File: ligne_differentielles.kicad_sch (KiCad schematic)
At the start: 2 parts, among them U11 AM26LS32ACDR

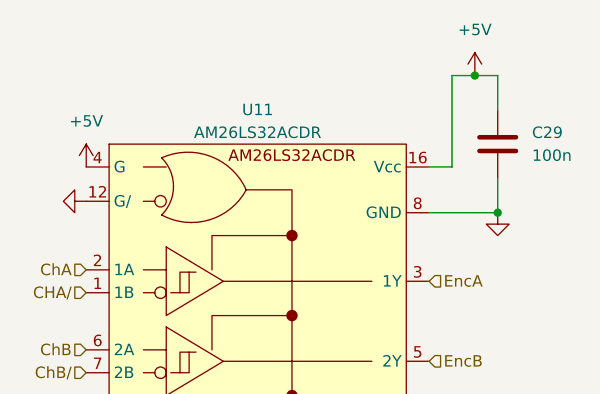
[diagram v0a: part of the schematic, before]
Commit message: reintroduction des mosfet (au lieu des demi-ponts en H), début routage
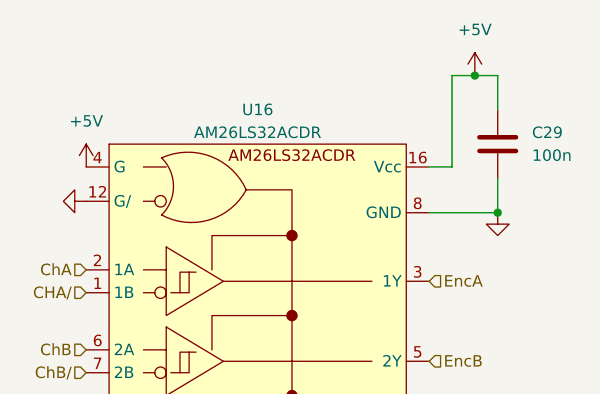
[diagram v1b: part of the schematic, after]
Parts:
- C29: footprint Capacitor_SMD:C_0402_1005Metric_Pad0.74x0.62mm_HandSolder -> Capacitor_SMD:C_0402_1005Metric
- renumbered U11 to U16
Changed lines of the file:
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@@
 		(dnp no)
 		(fields_autoplaced yes)
-		(property "Reference" "U11"
+		(property "Reference" "U16"
 			(at 140.97 62.23 0)
 			(effects
@@
 			(project "DRV8701_2Motors"
 				(path "/13741122-7bf4-473f-b117-422f29fb3018/5392043c-9573-4d80-aa55-c269598947da"
-					(reference "U12")
-					(unit 1)
-				)
-				(path "/13741122-7bf4-473f-b117-422f29fb3018/c8e44ded-48c4-4a1c-911e-f749872def21"
-					(reference "U11")
+					(reference "U17")
+					(unit 1)
+				)
+				(path "/13741122-7bf4-473f-b117-422f29fb3018/c8e44ded-48c4-4a1c-911e-f749872def21"
+					(reference "U16")
 					(unit 1)
 				)
@@
 			)
 		)
-		(property "Footprint" "Capacitor_SMD:C_0402_1005Metric_Pad0.74x0.62mm_HandSolder"
+		(property "Footprint" "Capacitor_SMD:C_0402_1005Metric"
 			(at 168.6052 69.85 0)
 			(effects
@@
 		(dnp no)
 		(fields_autoplaced yes)
-		(property "Reference" "#PWR052"
+		(property "Reference" "#PWR059"
 			(at 167.64 80.01 0)
 			(effects
@@
 			(project "DRV8701_2Motors"
 				(path "/13741122-7bf4-473f-b117-422f29fb3018/5392043c-9573-4d80-aa55-c269598947da"
-					(reference "#PWR056")
-					(unit 1)
-				)
-				(path "/13741122-7bf4-473f-b117-422f29fb3018/c8e44ded-48c4-4a1c-911e-f749872def21"
-					(reference "#PWR052")
+					(reference "#PWR063")
+					(unit 1)
+				)
+				(path "/13741122-7bf4-473f-b117-422f29fb3018/c8e44ded-48c4-4a1c-911e-f749872def21"
+					(reference "#PWR059")
 					(unit 1)
 				)
@@
 		(dnp no)
 		(fields_autoplaced yes)
-		(property "Reference" "#PWR050"
+		(property "Reference" "#PWR057"
 			(at 115.57 72.39 0)
 			(effects
@@
 			(project "DRV8701_2Motors"
 				(path "/13741122-7bf4-473f-b117-422f29fb3018/5392043c-9573-4d80-aa55-c269598947da"
-					(reference "#PWR054")
-					(unit 1)
-				)
-				(path "/13741122-7bf4-473f-b117-422f29fb3018/c8e44ded-48c4-4a1c-911e-f749872def21"
-					(reference "#PWR050")
+					(reference "#PWR061")
+					(unit 1)
+				)
+				(path "/13741122-7bf4-473f-b117-422f29fb3018/c8e44ded-48c4-4a1c-911e-f749872def21"
+					(reference "#PWR057")
 					(unit 1)
 				)
@@
 		(dnp no)
 		(fields_autoplaced yes)
-		(property "Reference" "#PWR049"
+		(property "Reference" "#PWR056"
 			(at 121.92 72.39 0)
 			(effects
@@
 			(project "DRV8701_2Motors"
 				(path "/13741122-7bf4-473f-b117-422f29fb3018/5392043c-9573-4d80-aa55-c269598947da"
-					(reference "#PWR053")
-					(unit 1)
-				)
-				(path "/13741122-7bf4-473f-b117-422f29fb3018/c8e44ded-48c4-4a1c-911e-f749872def21"
-					(reference "#PWR049")
+					(reference "#PWR060")
+					(unit 1)
+				)
+				(path "/13741122-7bf4-473f-b117-422f29fb3018/c8e44ded-48c4-4a1c-911e-f749872def21"
+					(reference "#PWR056")
 					(unit 1)
 				)
@@
 		(dnp no)
 		(fields_autoplaced yes)
-		(property "Reference" "#PWR051"
+		(property "Reference" "#PWR058"
 			(at 165.1 62.23 0)
 			(effects
@@
 			(project "DRV8701_2Motors"
 				(path "/13741122-7bf4-473f-b117-422f29fb3018/5392043c-9573-4d80-aa55-c269598947da"
-					(reference "#PWR055")
-					(unit 1)
-				)
-				(path "/13741122-7bf4-473f-b117-422f29fb3018/c8e44ded-48c4-4a1c-911e-f749872def21"
-					(reference "#PWR051")
-					(unit 1)
-				)
+					(reference "#PWR062")
+					(unit 1)
+				)
+				(path "/13741122-7bf4-473f-b117-422f29fb3018/c8e44ded-48c4-4a1c-911e-f749872def21"
+					(reference "#PWR058")
+					(unit 1)
+				)

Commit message: finalisation PCB
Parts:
- removed C29: 100n, Capacitor_SMD:C_0402_1005Metric, symbol Device:C
- removed U16: AM26LS32ACDR, Package_SO:SOIC-16_3.9x9.9mm_P1.27mm, symbol AM26LS32Ax:AM26LS32ACDR
- added C32: 100n, Capacitor_SMD:C_0402_1005Metric, symbol Device:C
- added R11, R13, R9: 120, Resistor_SMD:R_0201_0603Metric, symbol Device:R
- added U13: AM26LV32xD, Package_SO:SOIC-16_3.9x9.9mm_P1.27mm, symbol Interface:AM26LV32xD
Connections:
- net CHA/: now also R9.2, U13.1 (1B)
- net ChA: now also R9.1, U13.2 (1A)
- net ChB: now also R11.1, U13.6 (2A)
- net ChB/: now also R11.2, U13.7 (2B)
- net ChI: now also R13.1, U13.10 (3A)
- net ChI/: now also R13.2, U13.9 (3B)
- net EncA: now also U13.3 (1Y)
- net EncB: now also U13.5 (2Y)
- net EncI: now also U13.11 (3Y)
- net GND: now also C32.2, U13.12 (~{G}), U13.8 (GND)
- new net +3.3V: C32.1, U13.16 (VDD), U13.4 (G)
